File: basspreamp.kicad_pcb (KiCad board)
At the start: 2 copper layers, 62.2 x 44.5 mm, 27 parts, among them P1 INPUT, P2 OUTPUT, P3 Power, Q1 J201, U1 TL072

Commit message: PCB
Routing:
- removed copper zone on B.Cu, net Earth
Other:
- net class Default: via_dia 0.6 -> 1.2; via_drill 0.4 -> 0.8

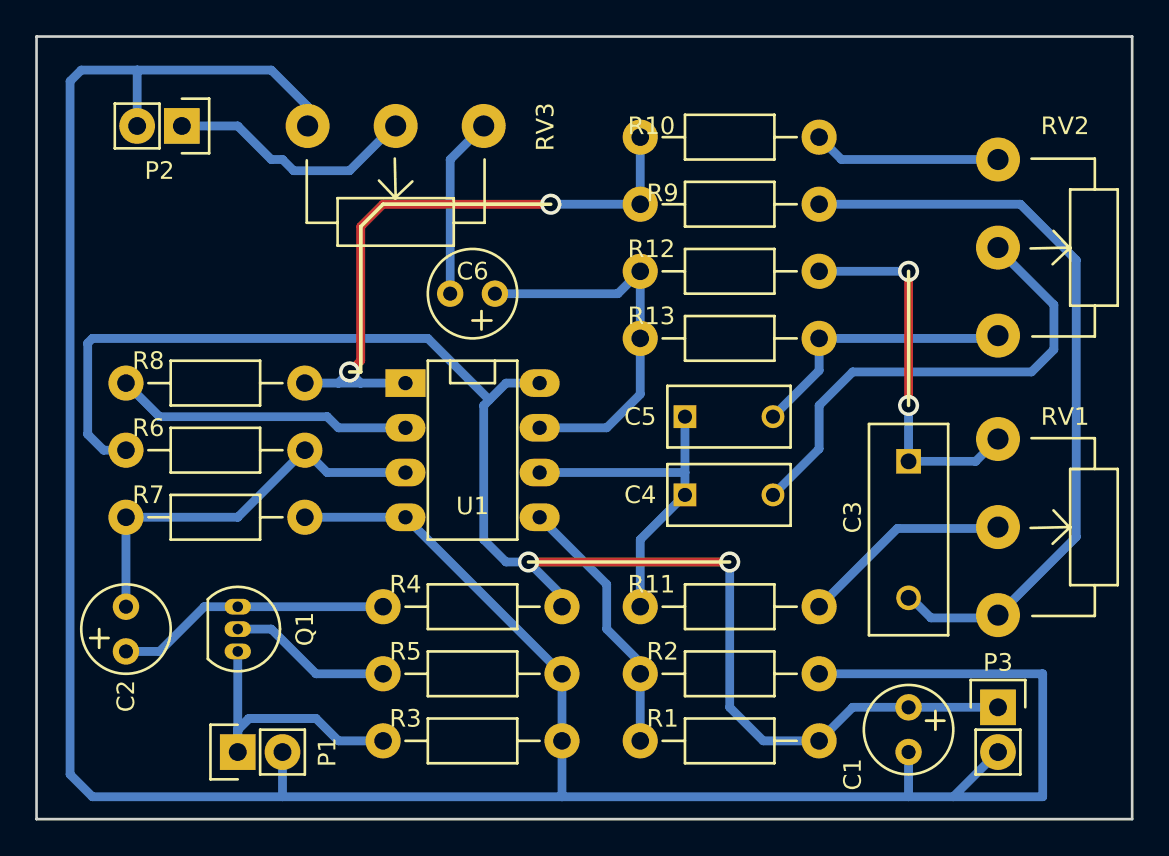
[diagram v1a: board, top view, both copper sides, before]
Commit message: Add filled zone to pcb, make prints
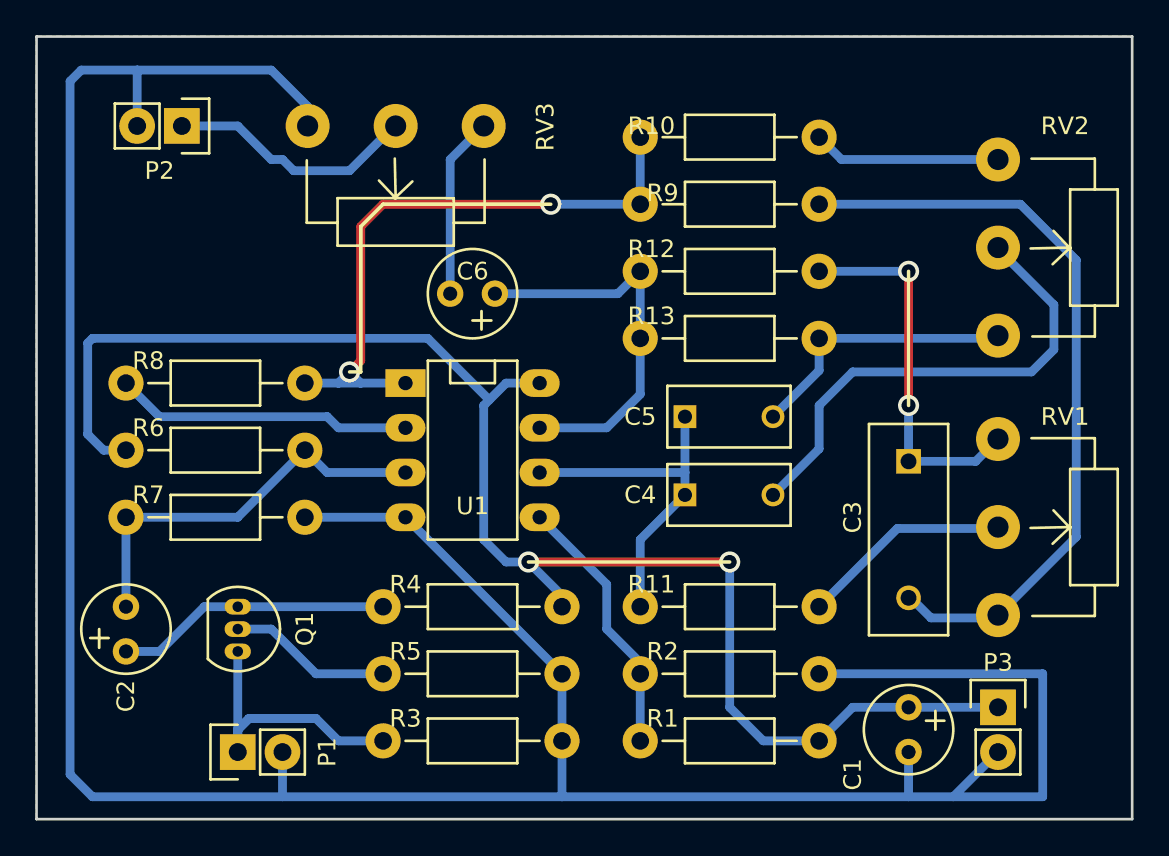
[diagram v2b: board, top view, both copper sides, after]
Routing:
- added copper zone on B.Cu, net Earth
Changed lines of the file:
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@@
-(kicad_pcb (version 4) (host pcbnew 0.201511182137+6324~38~ubuntu14.04.1-stable)
+(kicad_pcb (version 4) (host pcbnew 0.201511241017+6328~38~ubuntu14.04.1-stable)
   (general
     (links 45)
@@
   (via (at 145.415 107.95) (size 1.2) (drill 0.8) (layers F.Cu B.Cu) (net 2))
   (segment (start 145.415 107.95) (end 133.985 107.95) (width 0.5) (layer F.Cu) (net 2))
-  (via (at 133.985 107.95) (size 1.2) (drill 0.8) (layers F.Cu B.Cu) (net 2) (status 1000000))
+  (via (at 133.985 107.95) (size 1.2) (drill 0.8) (layers F.Cu B.Cu) (net 2))
   (segment (start 133.985 107.95) (end 132.715 107.95) (width 0.5) (layer B.Cu) (net 2))
   (segment (start 132.715 107.95) (end 131.445 106.68) (width 0.5) (layer B.Cu) (net 2))
@@
   (segment (start 150.495 83.82) (end 151.765 85.09) (width 0.5) (layer B.Cu) (net 19) (status 80010))
   (segment (start 151.765 85.09) (end 160.655 85.09) (width 0.5) (layer B.Cu) (net 19) (status 80020))
+  (zone (net 1) (net_name Earth) (layer B.Cu) (hatch edge 0.508)
+    (connect_pads (clearance 0.508))
+    (min_thickness 0.254)
+    (fill yes (arc_segments 16) (thermal_gap 0.508) (thermal_bridge_width 0.508))
+    (polygon
+      (pts
+        (xy 168.275 122.555) (xy 106.045 122.555) (xy 106.045 78.105) (xy 168.275 78.105) (xy 168.275 122.555)
+      )
+    )
+  )
 )
